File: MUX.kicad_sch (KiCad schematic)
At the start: 15 parts, among them IC401 ${DEVICE}

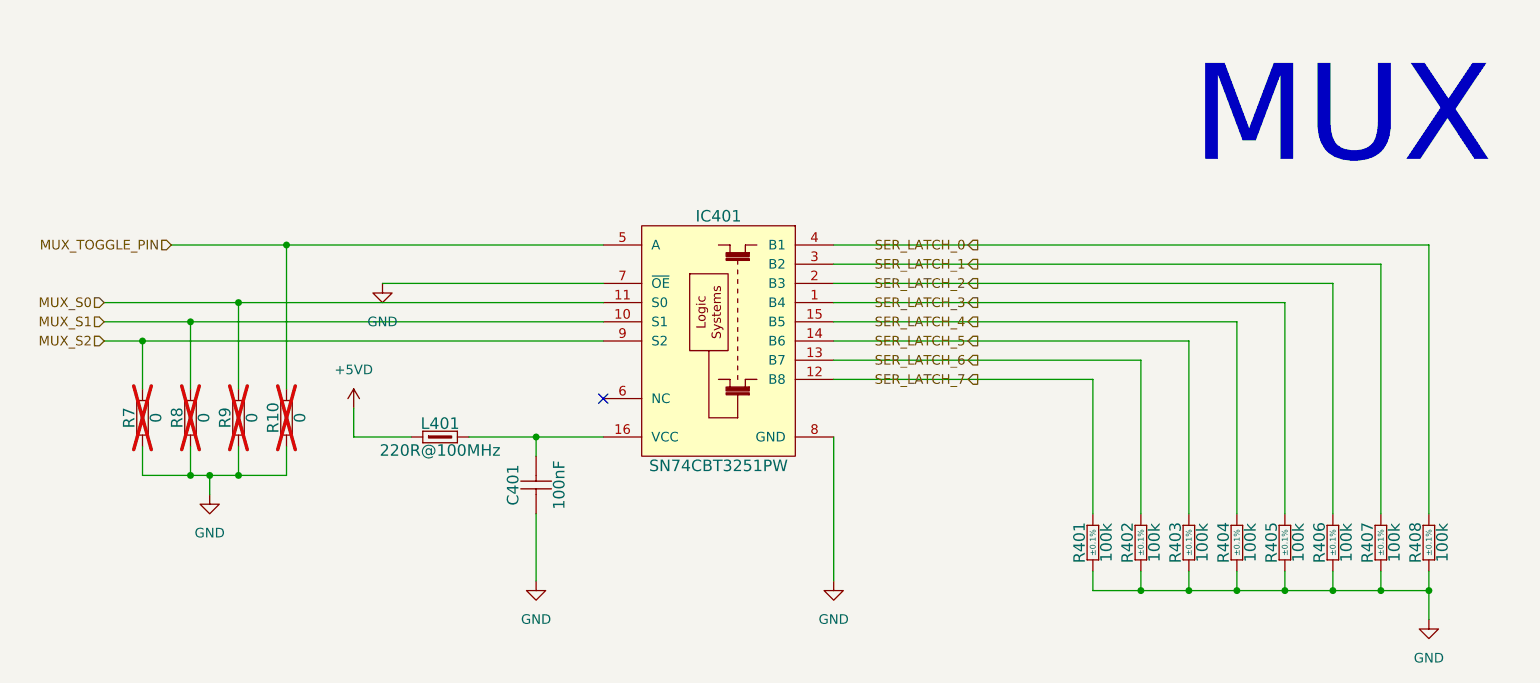
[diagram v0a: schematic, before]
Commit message: Rerouted PCB Logic part
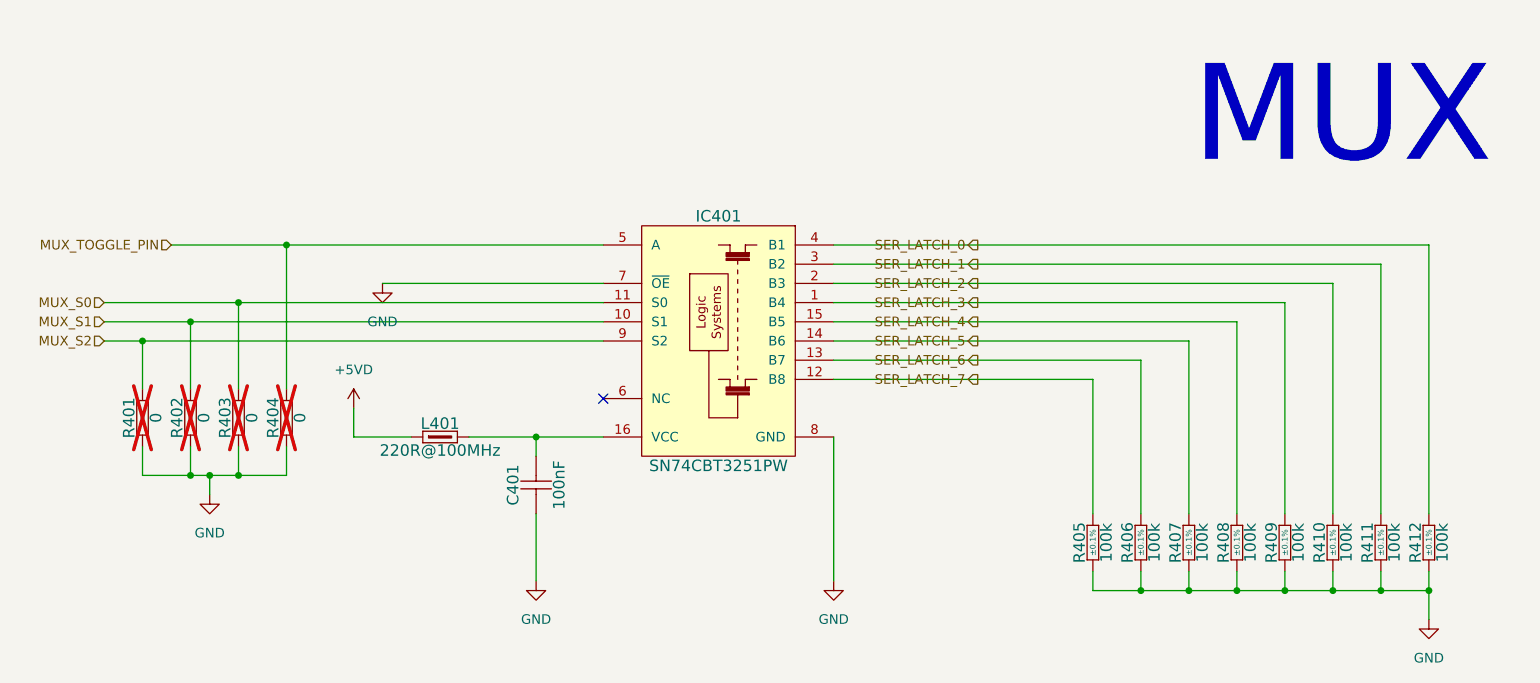
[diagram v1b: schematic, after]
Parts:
- renumbered R7 to R401, R8 to R402, R9 to R403, R10 to R404, R401 to R405, R402 to R406, R403 to R407, R404 to R408, R405 to R409, R406 to R410, R407 to R411, R408 to R412
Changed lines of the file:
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@@
 		(dnp no)
 		(fields_autoplaced yes)
-		(property "Reference" "#PWR0403"
+		(property "Reference" "#PWR0404"
 			(at 102.87 121.92 0)
 			(effects
@@
 			(project "8CH_Analog_Front_END"
 				(path "/41597329-5145-432a-9041-5bc2cec82d9b/1f5c05d6-380a-4bfc-9d7d-166f3f7ecba4"
-					(reference "#PWR0403")
+					(reference "#PWR0404")
 					(unit 1)
 				)
@@
 		(dnp no)
 		(fields_autoplaced yes)
-		(property "Reference" "#PWR0404"
+		(property "Reference" "#PWR0405"
 			(at 142.24 121.92 0)
 			(effects
@@
 			(project "8CH_Analog_Front_END"
 				(path "/41597329-5145-432a-9041-5bc2cec82d9b/1f5c05d6-380a-4bfc-9d7d-166f3f7ecba4"
-					(reference "#PWR0404")
+					(reference "#PWR0405")
 					(unit 1)
 				)
@@
 		(on_board yes)
 		(dnp yes)
-		(property "Reference" "R8"
+		(property "Reference" "R402"
 			(at 55.372 93.98 0)
 			(effects
@@
 			(project "8CH_Analog_Front_END"
 				(path "/41597329-5145-432a-9041-5bc2cec82d9b/1f5c05d6-380a-4bfc-9d7d-166f3f7ecba4"
-					(reference "R8")
+					(reference "R402")
 					(unit 1)
 				)
@@
 		(on_board yes)
 		(dnp no)
-		(property "Reference" "R408"
+		(property "Reference" "R412"
 			(at 219.202 110.49 0)
 			(effects
@@
 			(project "8CH_Analog_Front_END"
 				(path "/41597329-5145-432a-9041-5bc2cec82d9b/1f5c05d6-380a-4bfc-9d7d-166f3f7ecba4"
-					(reference "R408")
+					(reference "R412")
 					(unit 1)
 				)
@@
 		(on_board yes)
 		(dnp yes)
-		(property "Reference" "R7"
+		(property "Reference" "R401"
 			(at 49.022 93.98 0)
 			(effects
@@
 			(project "8CH_Analog_Front_END"
 				(path "/41597329-5145-432a-9041-5bc2cec82d9b/1f5c05d6-380a-4bfc-9d7d-166f3f7ecba4"
-					(reference "R7")
+					(reference "R401")
 					(unit 1)
 				)
@@
 		(on_board yes)
 		(dnp no)
-		(property "Reference" "R402"
+		(property "Reference" "R406"
 			(at 181.102 110.49 0)
 			(effects
@@
 			(project "8CH_Analog_Front_END"
 				(path "/41597329-5145-432a-9041-5bc2cec82d9b/1f5c05d6-380a-4bfc-9d7d-166f3f7ecba4"
-					(reference "R402")
+					(reference "R406")
 					(unit 1)
 				)
@@
 		(on_board yes)
 		(dnp yes)
-		(property "Reference" "R9"
+		(property "Reference" "R403"
 			(at 61.722 93.98 0)
 			(effects
@@
 			(project "8CH_Analog_Front_END"
 				(path "/41597329-5145-432a-9041-5bc2cec82d9b/1f5c05d6-380a-4bfc-9d7d-166f3f7ecba4"
-					(reference "R9")
+					(reference "R403")
 					(unit 1)
 				)
@@
 		(on_board yes)
 		(dnp no)
-		(property "Reference" "R407"
+		(property "Reference" "R411"
 			(at 212.852 110.49 0)
 			(effects
@@
 			(project "8CH_Analog_Front_END"
 				(path "/41597329-5145-432a-9041-5bc2cec82d9b/1f5c05d6-380a-4bfc-9d7d-166f3f7ecba4"
-					(reference "R407")
+					(reference "R411")
 					(unit 1)
 				)
@@
 		(on_board yes)
 		(dnp no)
-		(property "Reference" "R403"
+		(property "Reference" "R407"
 			(at 187.452 110.49 0)
 			(effects
@@
 			(project "8CH_Analog_Front_END"
 				(path "/41597329-5145-432a-9041-5bc2cec82d9b/1f5c05d6-380a-4bfc-9d7d-166f3f7ecba4"
-					(reference "R403")
+					(reference "R407")
 					(unit 1)
 				)
@@
 		(dnp no)
 		(fields_autoplaced yes)
-		(property "Reference" "#PWR07"
+		(property "Reference" "#PWR0401"
 			(at 59.69 110.49 0)
 			(effects
@@
 			(project "8CH_Analog_Front_END"
 				(path "/41597329-5145-432a-9041-5bc2cec82d9b/1f5c05d6-380a-4bfc-9d7d-166f3f7ecba4"
-					(reference "#PWR07")
+					(reference "#PWR0401")
 					(unit 1)
 				)
@@
 		(on_board yes)
 		(dnp no)
-		(property "Reference" "R401"
+		(property "Reference" "R405"
 			(at 174.752 110.49 0)
 			(effects
@@
 			(project "8CH_Analog_Front_END"
 				(path "/41597329-5145-432a-9041-5bc2cec82d9b/1f5c05d6-380a-4bfc-9d7d-166f3f7ecba4"
-					(reference "R401")
+					(reference "R405")
 					(unit 1)
 				)
@@
 		(dnp no)
 		(fields_autoplaced yes)
-		(property "Reference" "#PWR0401"
+		(property "Reference" "#PWR0403"
 			(at 82.55 82.55 0)
 			(effects
@@
 			(project "8CH_Analog_Front_END"
 				(path "/41597329-5145-432a-9041-5bc2cec82d9b/1f5c05d6-380a-4bfc-9d7d-166f3f7ecba4"
-					(reference "#PWR0401")
+					(reference "#PWR0403")
 					(unit 1)
 				)
@@
 		(on_board yes)
 		(dnp no)
-		(property "Reference" "R406"
+		(property "Reference" "R410"
 			(at 206.502 110.49 0)
 			(effects
@@
 			(project "8CH_Analog_Front_END"
 				(path "/41597329-5145-432a-9041-5bc2cec82d9b/1f5c05d6-380a-4bfc-9d7d-166f3f7ecba4"
-					(reference "R406")
+					(reference "R410")
 					(unit 1)
 				)
@@
 		(on_board yes)
 		(dnp no)
-		(property "Reference" "R405"
+		(property "Reference" "R409"
 			(at 200.152 110.49 0)
 			(effects
@@
 			(project "8CH_Analog_Front_END"
 				(path "/41597329-5145-432a-9041-5bc2cec82d9b/1f5c05d6-380a-4bfc-9d7d-166f3f7ecba4"
-					(reference "R405")
+					(reference "R409")
 					(unit 1)
 				)
@@
 		(on_board yes)
 		(dnp no)
-		(property "Reference" "R404"
+		(property "Reference" "R408"
 			(at 193.802 110.49 0)
 			(effects
@@
 			(project "8CH_Analog_Front_END"
 				(path "/41597329-5145-432a-9041-5bc2cec82d9b/1f5c05d6-380a-4bfc-9d7d-166f3f7ecba4"
-					(reference "R404")
+					(reference "R408")
 					(unit 1)
 				)
@@
 		(on_board yes)
 		(dnp yes)
-		(property "Reference" "R10"
+		(property "Reference" "R404"
 			(at 68.072 93.98 0)
 			(effects
@@
 			(project "8CH_Analog_Front_END"
 				(path "/41597329-5145-432a-9041-5bc2cec82d9b/1f5c05d6-380a-4bfc-9d7d-166f3f7ecba4"
-					(reference "R10")
+					(reference "R404")
 					(unit 1)
 				)
@@
 		(dnp no)
 		(fields_autoplaced yes)
-		(property "Reference" "#PWR0405"
+		(property "Reference" "#PWR0406"
 			(at 220.98 127 0)
 			(effects
@@
 			(project "8CH_Analog_Front_END"
 				(path "/41597329-5145-432a-9041-5bc2cec82d9b/1f5c05d6-380a-4bfc-9d7d-166f3f7ecba4"
-					(reference "#PWR0405")
+					(reference "#PWR0406")
 					(unit 1)
 				)
